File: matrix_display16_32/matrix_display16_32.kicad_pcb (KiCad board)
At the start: 2 copper layers, 96.5 x 45.7 mm, 33 parts, among them J1 Conn_01x05_Male, U1 MAX7219, U10 Matrix_LED, U11 Matrix_LED, U12 Matrix_LED, U13 Matrix_LED, U14 Matrix_LED, U15 Matrix_LED, U16 Matrix_LED, U2 MAX7219, U3 MAX7219, U4 MAX7219, U5 MAX7219, U6 MAX7219, U7 MAX7219, U8 MAX7219, U9 Matrix_LED

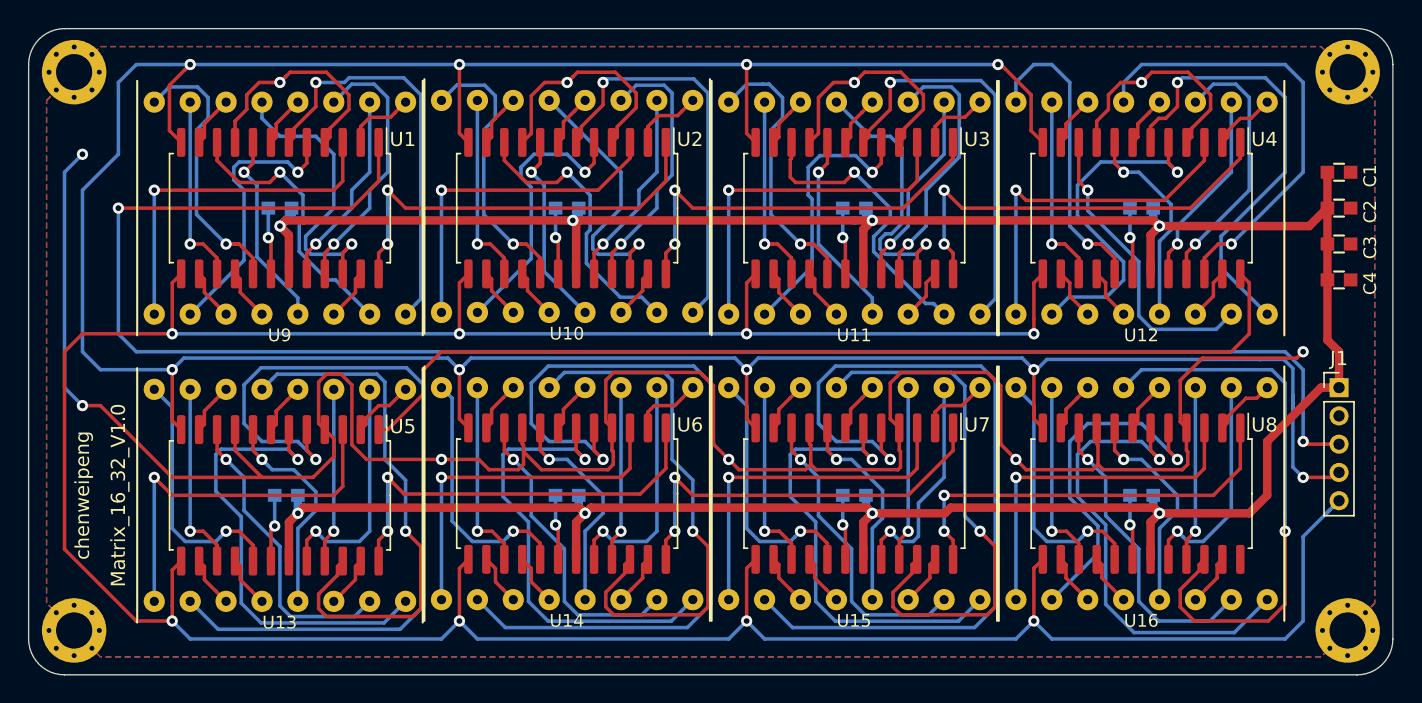
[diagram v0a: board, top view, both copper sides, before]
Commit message: 修改点阵铜柱洞3.5MM 修改连接接口2.54MM
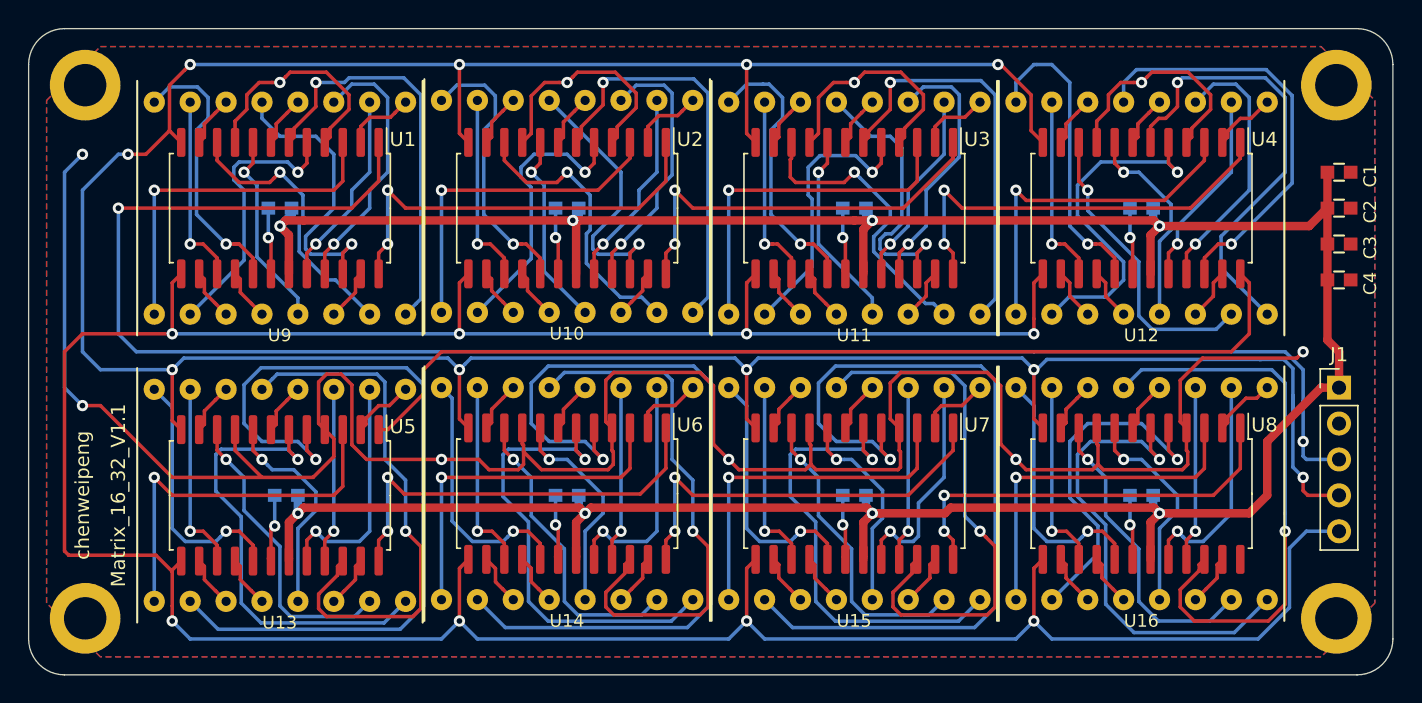
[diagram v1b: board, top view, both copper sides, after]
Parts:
- removed the REF** at (187.3, 86.9)
- removed the REF** at (187.3, 126.4)
- removed the REF** at (97.2, 126.4)
- removed the REF** at (97.2, 86.9)
- added REF**: hanpan, WDebug_DAPLink:hanpan, F.Cu at (186.6, 91.4)
- added REF**: hanpan, WDebug_DAPLink:hanpan, F.Cu at (186.7, 130.2)
- added REF**: hanpan, WDebug_DAPLink:hanpan, F.Cu at (97.8, 130.2)
- added REF**: hanpan, WDebug_DAPLink:hanpan, F.Cu at (97.8, 91.6)
- J1: footprint Connector_PinHeader_2.00mm:PinHeader_1x05_P2.00mm_Vertical -> Connector_PinHeader_2.54mm:PinHeader_1x05_P2.54mm_Vertical
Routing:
- net /CS: track 226.1 -> 220.7 mm, vias 9 -> 10
- net /CLK: track 224.2 -> 219.7 mm
- net /4_SEGDP: track 32.1 -> 30.2 mm
- net /DIN: track 123.4 -> 124.7 mm
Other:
- board text added: "Matrix_16_32_V1.1"
- board text removed: "Matrix_16_32_V1.0"
